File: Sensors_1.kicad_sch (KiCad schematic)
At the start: 24 parts, among them U10 LSM6DS3, U11 MPU-6500, U12 BMI270, U3 Ai-Thinker-Ra-01, U8 AT24C256, U9 Ai-Thinker-Ra-01SH

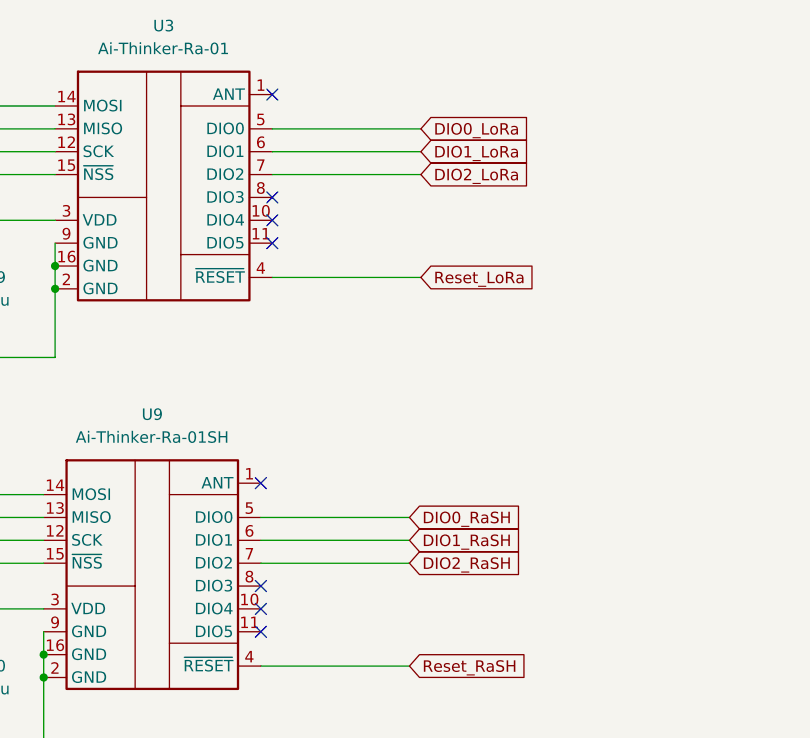
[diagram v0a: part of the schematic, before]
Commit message: feat: проведены все внешние линии и лдини связи с модулями LoRa
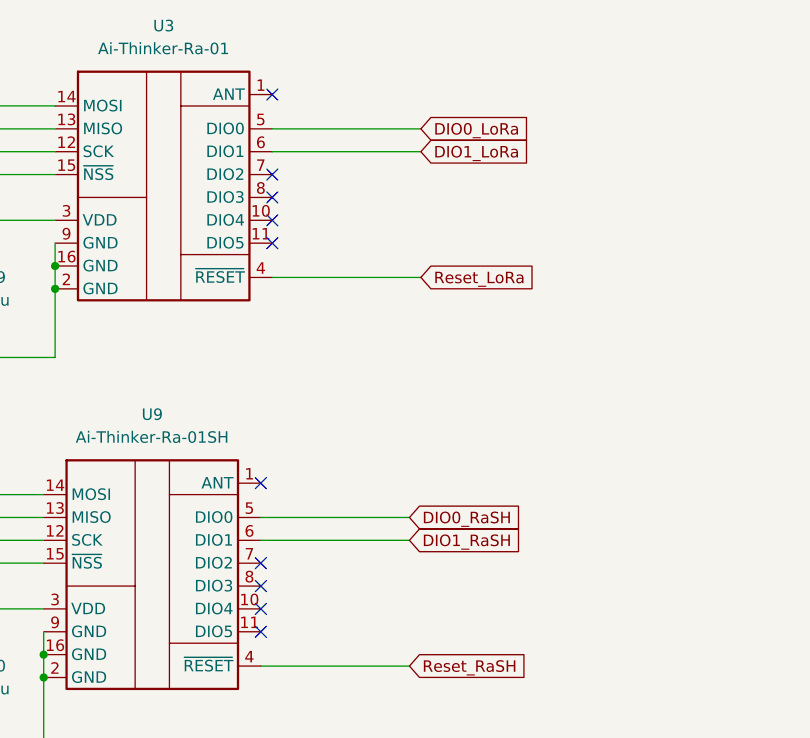
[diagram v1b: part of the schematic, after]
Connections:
- net DIO2_LoRa: no longer names the net of U3.7 (DIO2)
- net DIO2_RaSH: no longer names the net of U9.7 (DIO2)
- no-connect marks 14 -> 16
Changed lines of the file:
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@@
+	)
+	(no_connect
+		(at 87.63 39.37)
 	)
 	(no_connect
@@
 	)
 	(no_connect
+		(at 86.36 82.55)
+	)
+	(no_connect
 		(at 182.88 120.65)
 	)
@@
 	(wire
 		(pts
-			(xy 87.63 39.37) (xy 104.14 39.37)
-		)
-		(stroke
-			(width 0)
-			(type default)
-		)
-	)
-	(wire
-		(pts
 			(xy 172.72 130.81) (xy 182.88 130.81)
 		)
@@
 		(pts
 			(xy 242.57 125.73) (xy 242.57 127)
-		)
-		(stroke
-			(width 0)
-			(type default)
-		)
-	)
-	(wire
-		(pts
-			(xy 86.36 82.55) (xy 102.87 82.55)
 		)
 		(stroke
@@
 		)
 	)
-	(global_label "DIO2_RaSH"
-		(shape input)
-		(at 102.87 82.55 0)
-		(fields_autoplaced yes)
-		(effects
-			(font
-				(size 1.27 1.27)
-			)
-			(justify left)
-		)
-		(property "Intersheetrefs" "${INTERSHEET_REFS}"
-			(at 116.1966 82.55 0)
-			(hide yes)
-			(show_name no)
-			(do_not_autoplace no)
-			(effects
-				(font
-					(size 1.27 1.27)
-				)
-				(justify left)
-			)
-		)
-	)
 	(global_label "LSM_SCLK"
 		(shape input)
@@
 			)
 		)
-	)
-	(global_label "DIO2_LoRa"
-		(shape input)
-		(at 104.14 39.37 0)
-		(fields_autoplaced yes)
-		(effects
-			(font
-				(size 1.27 1.27)
-			)
-			(justify left)
-		)
-		(property "Intersheetrefs" "${INTERSHEET_REFS}"
-			(at 117.1037 39.37 0)
-			(hide yes)
-			(show_name no)
-			(do_not_autoplace no)
-			(effects
-				(font
-					(size 1.27 1.27)
-				)
-				(justify left)
-			)
-		)
